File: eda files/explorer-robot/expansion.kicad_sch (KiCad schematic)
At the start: 11 parts, among them J10 EXP.DATA, J9 EXP.PWR, U10 TPS22917DBV

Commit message: ``` Move AI camera branch to 3.3 V rail
The Grove Vision AI V2 module used here requires a 3.3 V input,
so powering it from the switched 5 V branch would over-voltage it.
Point U9 VIN at +3.3V; the TPS22917, footprint and control are
unchanged.

Also bump the 5 V inductor to 15 µH/3 A, swap the catch diode,
clean up schematic wiring and add no-connects on unused pins.
Document the decision in ADR-0025 and update ADR-0019, ADR-0021
and CONTEXT.md.
```
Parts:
- added C61: 10u, Capacitor_SMD:C_0805_2012Metric, symbol Device:C
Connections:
- net GND: now also C61.2
- net at C57.2, J9.1 (Pin_1), R21.1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: now also C61.1
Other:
- moved on the sheet: R23, R24, R25, R26

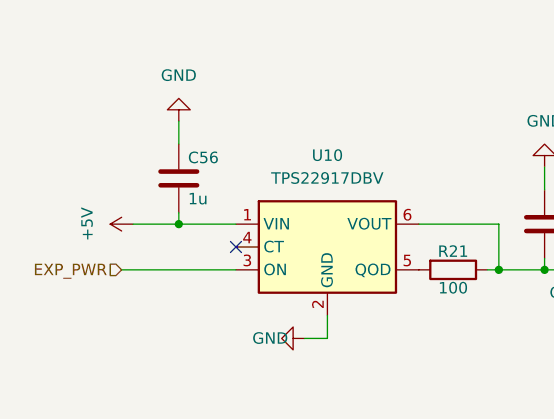
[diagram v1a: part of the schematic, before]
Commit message: Add 1 nF CT capacitors to TPS22917 load switches
Specify C29/C30/C67/C68 on the LiDAR, AI camera, expansion and
panel branches to give a controlled rise and limit inrush. Update
ADRs 0010, 0021, 0024 and 0027 and CONTEXT.md to match, rework the
affected schematics, and swap the inductor footprint to the
EasyEDA SLO0618H part.
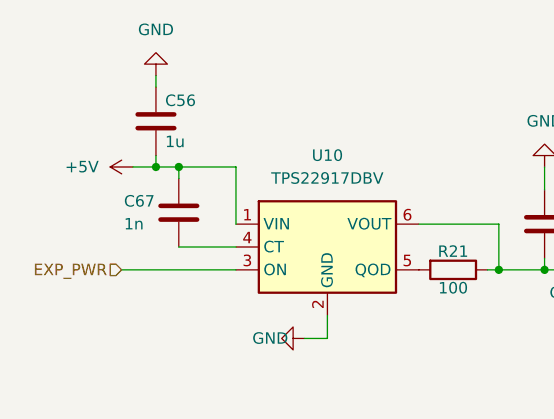
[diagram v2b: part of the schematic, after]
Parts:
- added C67: 1n, Capacitor_SMD:C_0603_1608Metric, symbol Device:C
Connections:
- net +5V: now also C67.2
- net at U10.4 (CT): now also C67.1
- no-connect marks 1 -> 0
